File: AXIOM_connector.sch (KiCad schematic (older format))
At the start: 12 parts, among them U1001 BR24G04NUX

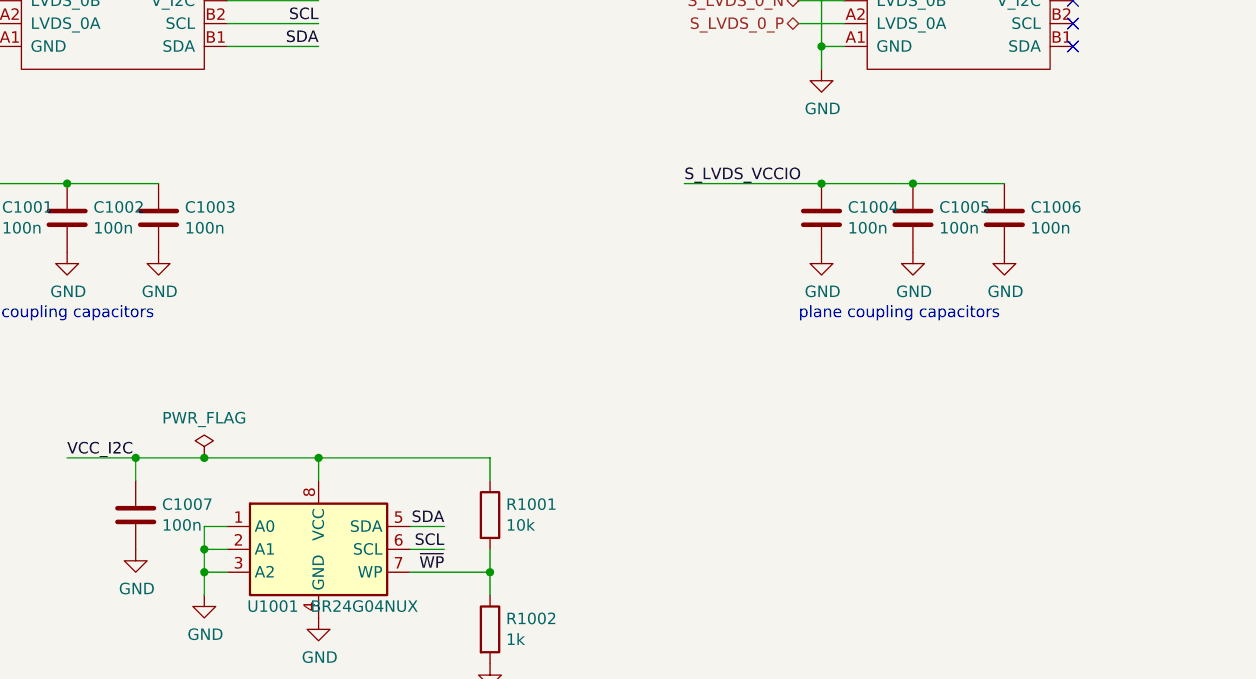
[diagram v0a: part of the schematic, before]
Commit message: route +3V3 net and add bypass capacitor
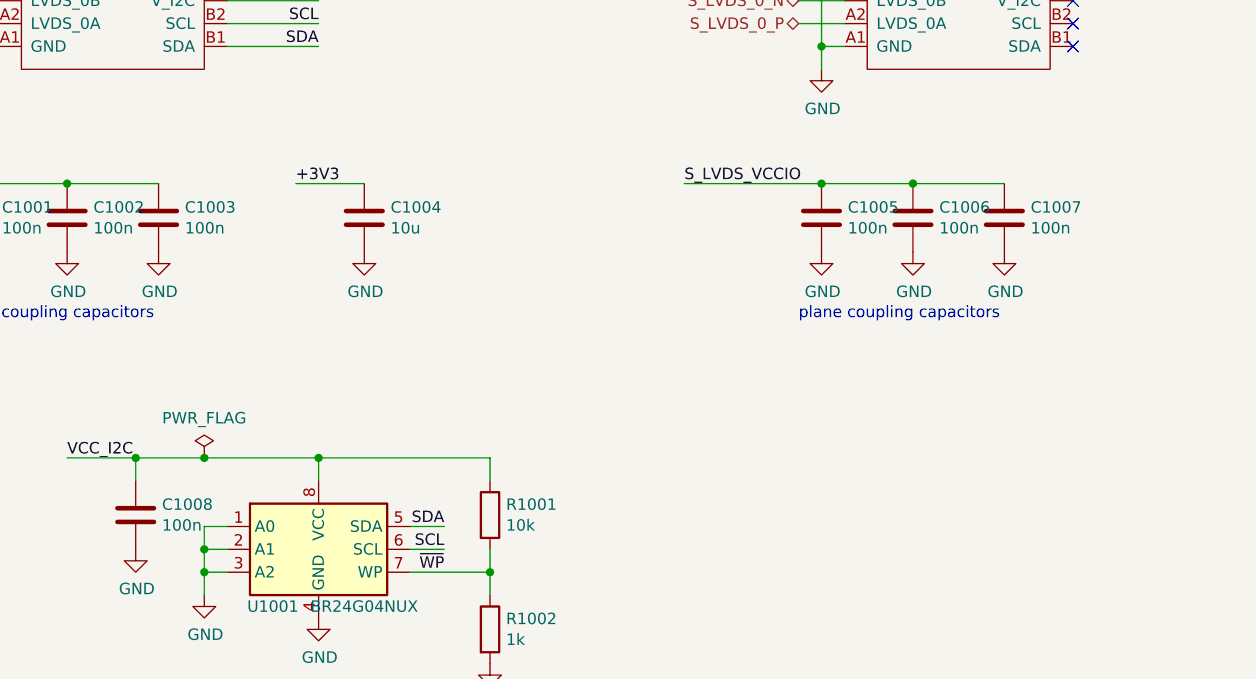
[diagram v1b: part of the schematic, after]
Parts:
- added C1004: 10u, Capacitor_SMD:C_0402_1005Metric, symbol Device:C
- renumbered C1004 to C1005, C1005 to C1006, C1006 to C1007, C1007 to C1008
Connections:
- net +3V3: now also C1004.1
- net GND: now also C1004.2
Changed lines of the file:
@@
 $EndComp
 $Comp
-L power:GND #PWR01013
+L power:GND #PWR01014
 U 1 1 5AFBF1A7
 P 4400 6800
-F 0 "#PWR01013" H 4400 6550 50  0001 C CNN
+F 0 "#PWR01014" H 4400 6550 50  0001 C CNN
 F 1 "GND" H 4405 6627 50  0000 C CNN
 F 2 "" H 4400 6800 50  0001 C CNN
@@
 $EndComp
 $Comp
-L power:GND #PWR01012
+L power:GND #PWR01013
 U 1 1 5AFBF1E7
 P 3900 6700
-F 0 "#PWR01012" H 3900 6450 50  0001 C CNN
+F 0 "#PWR01013" H 3900 6450 50  0001 C CNN
 F 1 "GND" H 3905 6527 50  0000 C CNN
 F 2 "" H 3900 6700 50  0001 C CNN
@@
 	3900 6600 3900 6700
 $Comp
-L Device:C C1007
+L Device:C C1008
 U 1 1 5AFC04F5
 P 3600 6350
-F 0 "C1007" H 3715 6396 50  0000 L CNN
+F 0 "C1008" H 3715 6396 50  0000 L CNN
 F 1 "100n" H 3715 6305 50  0000 L CNN
 F 2 "Capacitor_SMD:C_0402_1005Metric" H 3638 6200 50  0001 C CNN
@@
 $EndComp
 $Comp
-L power:GND #PWR01011
+L power:GND #PWR01012
 U 1 1 5AFC0567
 P 3600 6500
-F 0 "#PWR01011" H 3600 6250 50  0001 C CNN
+F 0 "#PWR01012" H 3600 6250 50  0001 C CNN
 F 1 "GND" H 3605 6327 50  0000 C CNN
 F 2 "" H 3600 6500 50  0001 C CNN
@@
 $EndComp
 $Comp
-L power:GND #PWR01014
+L power:GND #PWR01015
 U 1 1 5AFC3D07
 P 5150 7000
-F 0 "#PWR01014" H 5150 6750 50  0001 C CNN
+F 0 "#PWR01015" H 5150 6750 50  0001 C CNN
 F 1 "GND" H 5155 6827 50  0000 C CNN
 F 2 "" H 5150 7000 50  0001 C CNN
@@
 Connection ~ 3300 4900
 $Comp
-L Device:C C1004
+L Device:C C1005
 U 1 1 5B9999D8
 P 6600 5050
-F 0 "C1004" H 6715 5096 50  0000 L CNN
+F 0 "C1005" H 6715 5096 50  0000 L CNN
 F 1 "100n" H 6715 5005 50  0000 L CNN
 F 2 "Capacitor_SMD:C_0402_1005Metric" H 6638 4900 50  0001 C CNN
@@
 $EndComp
 $Comp
-L power:GND #PWR01008
+L power:GND #PWR01009
 U 1 1 5B9999DE
 P 6600 5200
-F 0 "#PWR01008" H 6600 4950 50  0001 C CNN
+F 0 "#PWR01009" H 6600 4950 50  0001 C CNN
 F 1 "GND" H 6605 5027 50  0000 C CNN
 F 2 "" H 6600 5200 50  0001 C CNN
@@
 	6000 4900 6600 4900
 $Comp
-L Device:C C1005
+L Device:C C1006
 U 1 1 5B9999E6
 P 7000 5050
-F 0 "C1005" H 7115 5096 50  0000 L CNN
+F 0 "C1006" H 7115 5096 50  0000 L CNN
 F 1 "100n" H 7115 5005 50  0000 L CNN
 F 2 "Capacitor_SMD:C_0402_1005Metric" H 7038 4900 50  0001 C CNN
@@
 $EndComp
 $Comp
-L power:GND #PWR01009
+L power:GND #PWR01010
 U 1 1 5B9999EC
 P 7000 5200
-F 0 "#PWR01009" H 7000 4950 50  0001 C CNN
+F 0 "#PWR01010" H 7000 4950 50  0001 C CNN
 F 1 "GND" H 7005 5027 50  0000 C CNN
 F 2 "" H 7000 5200 50  0001 C CNN
@@
 $EndComp
 $Comp
-L Device:C C1006
+L Device:C C1007
 U 1 1 5B9999F2
 P 7400 5050
-F 0 "C1006" H 7515 5096 50  0000 L CNN
+F 0 "C1007" H 7515 5096 50  0000 L CNN
 F 1 "100n" H 7515 5005 50  0000 L CNN
 F 2 "Capacitor_SMD:C_0402_1005Metric" H 7438 4900 50  0001 C CNN
@@
 $EndComp
 $Comp
-L power:GND #PWR01010
+L power:GND #PWR01011
 U 1 1 5B9999F8
 P 7400 5200
-F 0 "#PWR01010" H 7400 4950 50  0001 C CNN
+F 0 "#PWR01011" H 7400 4950 50  0001 C CNN
 F 1 "GND" H 7405 5027 50  0000 C CNN
 F 2 "" H 7400 5200 50  0001 C CNN
@@
 Text Notes 6500 5500 0    50   ~ 0
 plane coupling capacitors
+Wire Wire Line
+	4600 4900 4300 4900
+Text Label 4300 4900 0    50   ~ 0
++3V3
+$Comp
+L Device:C C1004
+U 1 1 5B4BBC86
+P 4600 5050
+F 0 "C1004" H 4715 5096 50  0000 L CNN
+F 1 "10u" H 4715 5005 50  0000 L CNN
+F 2 "Capacitor_SMD:C_0402_1005Metric" H 4638 4900 50  0001 C CNN
+F 3 "~" H 4600 5050 50  0001 C CNN
+	1    4600 5050
+	1    0    0    -1
+$EndComp
+$Comp
+L power:GND #PWR01008
+U 1 1 5B4BBCC0
+P 4600 5200
+F 0 "#PWR01008" H 4600 4950 50  0001 C CNN
+F 1 "GND" H 4605 5027 50  0000 C CNN
+F 2 "" H 4600 5200 50  0001 C CNN
+F 3 "" H 4600 5200 50  0001 C CNN
+	1    4600 5200
+	1    0    0    -1
+$EndComp
 $EndSCHEMATC

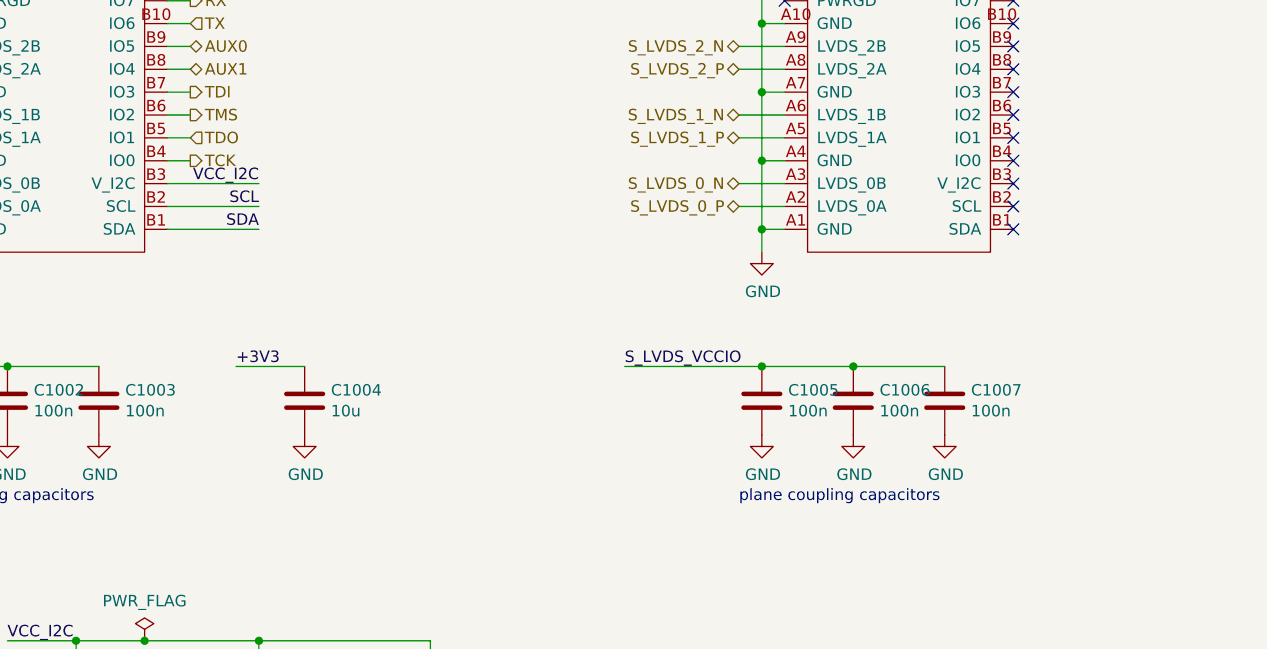
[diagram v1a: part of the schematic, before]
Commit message: move eeprom to south conector
also move the 5v->1,8v stepdown a bit to have space for the eeprom
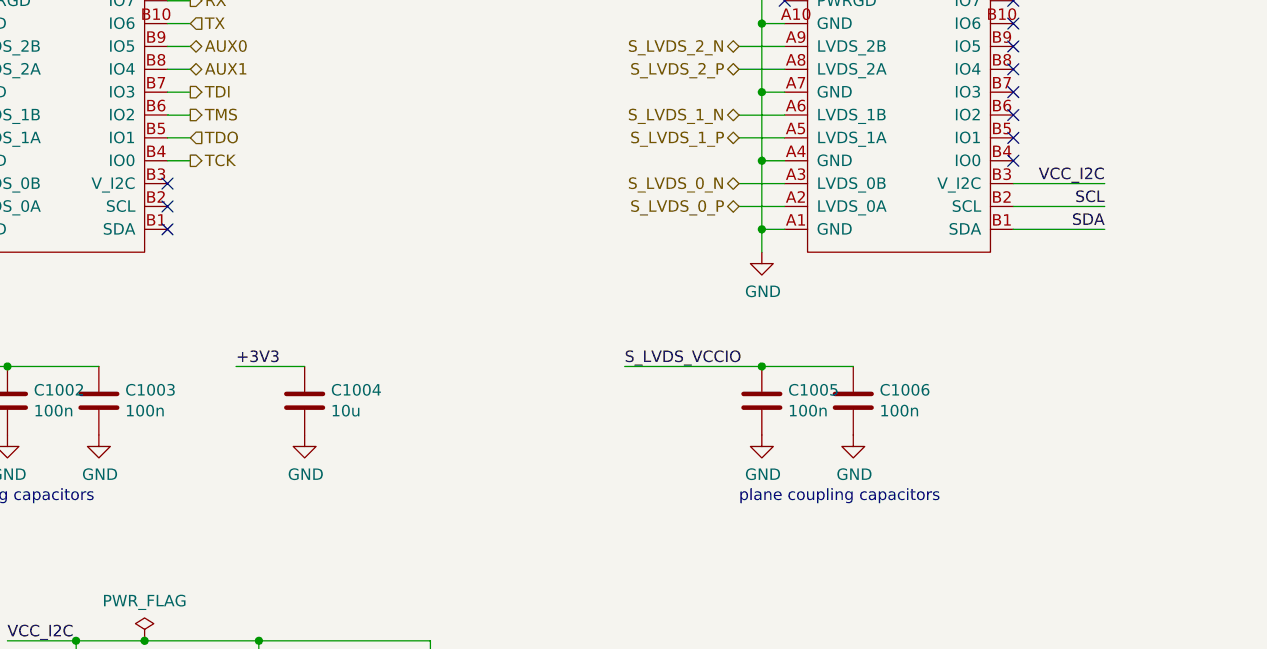
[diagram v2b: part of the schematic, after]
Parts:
- removed C1007: 100n, Capacitor_SMD:C_0402_1005Metric, symbol Device:C
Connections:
- net SCL: now also AXIOM_SOUTH1001.B2 (SCL); no longer AXIOM_NORTH1001.B2 (SCL)
- net SDA: now also AXIOM_SOUTH1001.B1 (SDA); no longer AXIOM_NORTH1001.B1 (SDA)
- net VCC_I2C: now also AXIOM_SOUTH1001.B3 (V_I2C); no longer AXIOM_NORTH1001.B3 (V_I2C)
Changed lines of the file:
@@
 EESchema Schematic File Version 4
 LIBS:AXIOM-photonSDI-hw-cache
-EELAYER 26 0
+EELAYER 29 0
 EELAYER END
 $Descr A4 11693 8268
@@
 Wire Wire Line
 	7700 2800 7800 2800
-NoConn ~ 7700 4300
-NoConn ~ 7700 4200
-NoConn ~ 7700 4100
-Wire Wire Line
-	4400 4300 4000 4300
-Wire Wire Line
-	4400 4200 4000 4200
-Wire Wire Line
-	4400 4100 4000 4100
-Text Label 4400 4100 2    50   ~ 0
+Wire Wire Line
+	8100 4300 7700 4300
+Wire Wire Line
+	8100 4200 7700 4200
+Wire Wire Line
+	8100 4100 7700 4100
+Text Label 8100 4100 2    50   ~ 0
 VCC_I2C
-Text Label 4400 4200 2    50   ~ 0
+Text Label 8100 4200 2    50   ~ 0
 SCL
-Text Label 4400 4300 2    50   ~ 0
+Text Label 8100 4300 2    50   ~ 0
 SDA
 $Comp
@@
 	1    0    0    -1
 $EndComp
-$Comp
-L Device:C C1007
-U 1 1 5B9999F2
-P 7400 5050
-F 0 "C1007" H 7515 5096 50  0000 L CNN
-F 1 "100n" H 7515 5005 50  0000 L CNN
-F 2 "Capacitor_SMD:C_0402_1005Metric" H 7438 4900 50  0001 C CNN
-F 3 "~" H 7400 5050 50  0001 C CNN
-	1    7400 5050
-	1    0    0    -1
-$EndComp
-$Comp
-L power:GND #PWR01011
-U 1 1 5B9999F8
-P 7400 5200
-F 0 "#PWR01011" H 7400 4950 50  0001 C CNN
-F 1 "GND" H 7405 5027 50  0000 C CNN
-F 2 "" H 7400 5200 50  0001 C CNN
-F 3 "" H 7400 5200 50  0001 C CNN
-	1    7400 5200
-	1    0    0    -1
-$EndComp
 Wire Wire Line
 	6600 4900 7000 4900
 Connection ~ 6600 4900
-Wire Wire Line
-	7000 4900 7400 4900
-Connection ~ 7000 4900
 Text Label 6000 4900 0    50   ~ 0
 S_LVDS_VCCIO
@@
 	1    0    0    -1
 $EndComp
+NoConn ~ 4000 4100
+NoConn ~ 4000 4200
+NoConn ~ 4000 4300
 $EndSCHEMATC

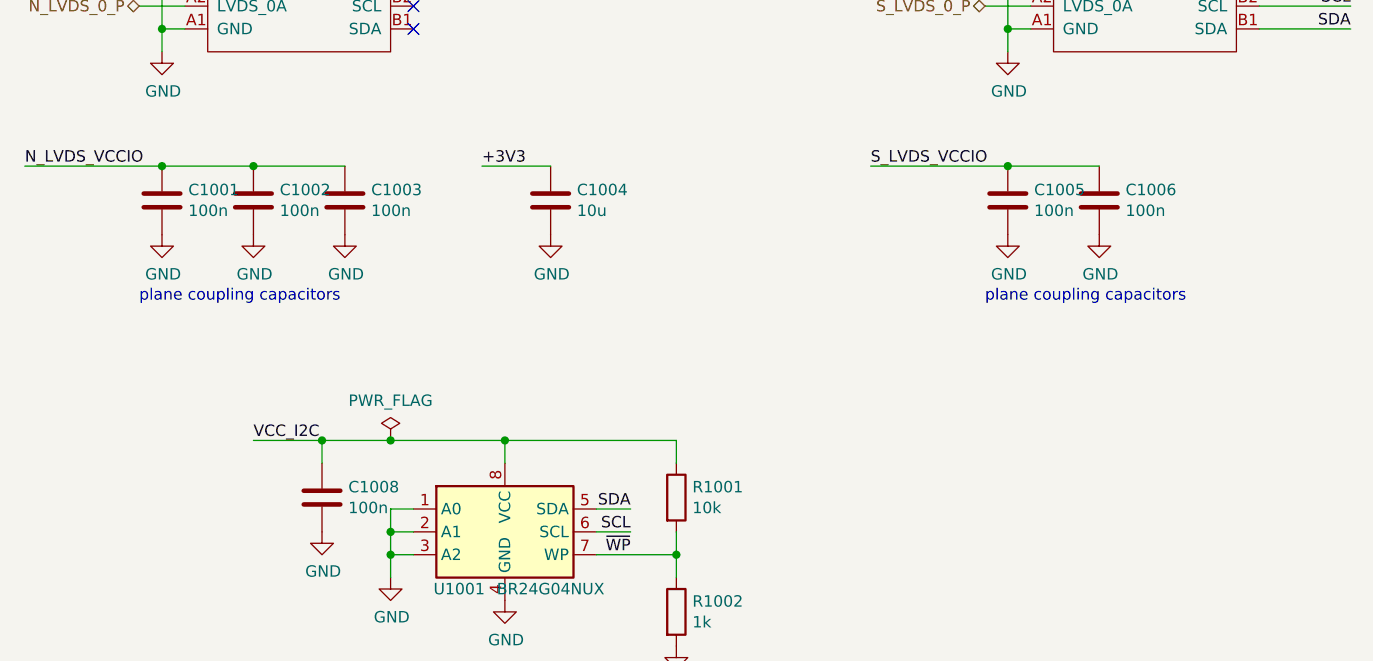
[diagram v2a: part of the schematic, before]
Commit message: rework plane coupling capacitors on axiom connector
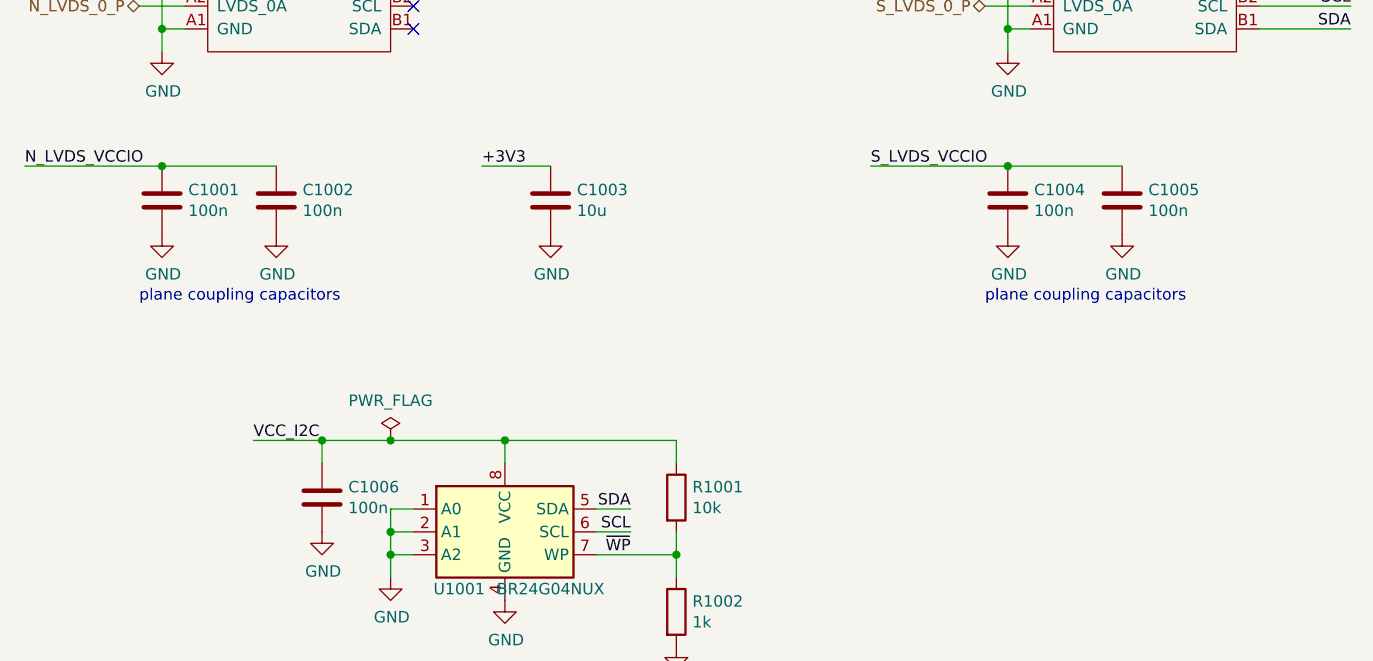
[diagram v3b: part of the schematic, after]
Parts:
- removed C1002: 100n, Capacitor_SMD:C_0402_1005Metric, symbol Device:C
- renumbered C1003 to C1002, C1004 to C1003, C1005 to C1004, C1006 to C1005, C1008 to C1006
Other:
- moved on the sheet: C1002, C1005
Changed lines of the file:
@@
 $EndComp
 $Comp
-L power:GND #PWR01014
+L power:GND #PWR01012
 U 1 1 5AFBF1A7
 P 4400 6800
-F 0 "#PWR01014" H 4400 6550 50  0001 C CNN
+F 0 "#PWR01012" H 4400 6550 50  0001 C CNN
 F 1 "GND" H 4405 6627 50  0000 C CNN
 F 2 "" H 4400 6800 50  0001 C CNN
@@
 $EndComp
 $Comp
-L power:GND #PWR01013
+L power:GND #PWR01011
 U 1 1 5AFBF1E7
 P 3900 6700
-F 0 "#PWR01013" H 3900 6450 50  0001 C CNN
+F 0 "#PWR01011" H 3900 6450 50  0001 C CNN
 F 1 "GND" H 3905 6527 50  0000 C CNN
 F 2 "" H 3900 6700 50  0001 C CNN
@@
 	3900 6600 3900 6700
 $Comp
-L Device:C C1008
+L Device:C C1006
 U 1 1 5AFC04F5
 P 3600 6350
-F 0 "C1008" H 3715 6396 50  0000 L CNN
+F 0 "C1006" H 3715 6396 50  0000 L CNN
 F 1 "100n" H 3715 6305 50  0000 L CNN
 F 2 "Capacitor_SMD:C_0402_1005Metric" H 3638 6200 50  0001 C CNN
@@
 $EndComp
 $Comp
-L power:GND #PWR01012
+L power:GND #PWR01010
 U 1 1 5AFC0567
 P 3600 6500
-F 0 "#PWR01012" H 3600 6250 50  0001 C CNN
+F 0 "#PWR01010" H 3600 6250 50  0001 C CNN
 F 1 "GND" H 3605 6327 50  0000 C CNN
 F 2 "" H 3600 6500 50  0001 C CNN
@@
 $EndComp
 $Comp
-L power:GND #PWR01015
+L power:GND #PWR01013
 U 1 1 5AFC3D07
 P 5150 7000
-F 0 "#PWR01015" H 5150 6750 50  0001 C CNN
+F 0 "#PWR01013" H 5150 6750 50  0001 C CNN
 F 1 "GND" H 5155 6827 50  0000 C CNN
 F 2 "" H 5150 7000 50  0001 C CNN
@@
 $Comp
 L Device:C C1002
-U 1 1 5B9079A6
-P 3300 5050
-F 0 "C1002" H 3415 5096 50  0000 L CNN
-F 1 "100n" H 3415 5005 50  0000 L CNN
-F 2 "Capacitor_SMD:C_0402_1005Metric" H 3338 4900 50  0001 C CNN
-F 3 "~" H 3300 5050 50  0001 C CNN
-	1    3300 5050
+U 1 1 5B90F3FB
+P 3400 5050
+F 0 "C1002" H 3515 5096 50  0000 L CNN
+F 1 "100n" H 3515 5005 50  0000 L CNN
+F 2 "Capacitor_SMD:C_0402_1005Metric" H 3438 4900 50  0001 C CNN
+F 3 "~" H 3400 5050 50  0001 C CNN
+	1    3400 5050
 	1    0    0    -1
 $EndComp
 $Comp
 L power:GND #PWR01006
-U 1 1 5B9079AD
-P 3300 5200
-F 0 "#PWR01006" H 3300 4950 50  0001 C CNN
-F 1 "GND" H 3305 5027 50  0000 C CNN
-F 2 "" H 3300 5200 50  0001 C CNN
-F 3 "" H 3300 5200 50  0001 C CNN
-	1    3300 5200
-	1    0    0    -1
-$EndComp
-$Comp
-L Device:C C1003
-U 1 1 5B90F3FB
-P 3700 5050
-F 0 "C1003" H 3815 5096 50  0000 L CNN
-F 1 "100n" H 3815 5005 50  0000 L CNN
-F 2 "Capacitor_SMD:C_0402_1005Metric" H 3738 4900 50  0001 C CNN
-F 3 "~" H 3700 5050 50  0001 C CNN
-	1    3700 5050
-	1    0    0    -1
-$EndComp
-$Comp
-L power:GND #PWR01007
 U 1 1 5B90F402
-P 3700 5200
-F 0 "#PWR01007" H 3700 4950 50  0001 C CNN
-F 1 "GND" H 3705 5027 50  0000 C CNN
-F 2 "" H 3700 5200 50  0001 C CNN
-F 3 "" H 3700 5200 50  0001 C CNN
-	1    3700 5200
-	1    0    0    -1
-$EndComp
-Wire Wire Line
-	2900 4900 3300 4900
+P 3400 5200
+F 0 "#PWR01006" H 3400 4950 50  0001 C CNN
+F 1 "GND" H 3405 5027 50  0000 C CNN
+F 2 "" H 3400 5200 50  0001 C CNN
+F 3 "" H 3400 5200 50  0001 C CNN
+	1    3400 5200
+	1    0    0    -1
+$EndComp
 Connection ~ 2900 4900
-Wire Wire Line
-	3300 4900 3700 4900
-Connection ~ 3300 4900
-$Comp
-L Device:C C1005
+$Comp
+L Device:C C1004
 U 1 1 5B9999D8
 P 6600 5050
-F 0 "C1005" H 6715 5096 50  0000 L CNN
+F 0 "C1004" H 6715 5096 50  0000 L CNN
 F 1 "100n" H 6715 5005 50  0000 L CNN
 F 2 "Capacitor_SMD:C_0402_1005Metric" H 6638 4900 50  0001 C CNN
@@
 $EndComp
 $Comp
-L power:GND #PWR01009
+L power:GND #PWR01008
 U 1 1 5B9999DE
 P 6600 5200
-F 0 "#PWR01009" H 6600 4950 50  0001 C CNN
+F 0 "#PWR01008" H 6600 4950 50  0001 C CNN
 F 1 "GND" H 6605 5027 50  0000 C CNN
 F 2 "" H 6600 5200 50  0001 C CNN
@@
 	6000 4900 6600 4900
 $Comp
-L Device:C C1006
+L Device:C C1005
 U 1 1 5B9999E6
-P 7000 5050
-F 0 "C1006" H 7115 5096 50  0000 L CNN
-F 1 "100n" H 7115 5005 50  0000 L CNN
-F 2 "Capacitor_SMD:C_0402_1005Metric" H 7038 4900 50  0001 C CNN
-F 3 "~" H 7000 5050 50  0001 C CNN
-	1    7000 5050
-	1    0    0    -1
-$EndComp
-$Comp
-L power:GND #PWR01010
+P 7100 5050
+F 0 "C1005" H 7215 5096 50  0000 L CNN
+F 1 "100n" H 7215 5005 50  0000 L CNN
+F 2 "Capacitor_SMD:C_0402_1005Metric" H 7138 4900 50  0001 C CNN
+F 3 "~" H 7100 5050 50  0001 C CNN
+	1    7100 5050
+	1    0    0    -1
+$EndComp
+$Comp
+L power:GND #PWR01009
 U 1 1 5B9999EC
-P 7000 5200
-F 0 "#PWR01010" H 7000 4950 50  0001 C CNN
-F 1 "GND" H 7005 5027 50  0000 C CNN
-F 2 "" H 7000 5200 50  0001 C CNN
-F 3 "" H 7000 5200 50  0001 C CNN
-	1    7000 5200
-	1    0    0    -1
-$EndComp
-Wire Wire Line
-	6600 4900 7000 4900
+P 7100 5200
+F 0 "#PWR01009" H 7100 4950 50  0001 C CNN
+F 1 "GND" H 7105 5027 50  0000 C CNN
+F 2 "" H 7100 5200 50  0001 C CNN
+F 3 "" H 7100 5200 50  0001 C CNN
+	1    7100 5200
+	1    0    0    -1
+$EndComp
+Wire Wire Line
+	6600 4900 7100 4900
 Connection ~ 6600 4900
 Text Label 6000 4900 0    50   ~ 0
@@
 +3V3
 $Comp
-L Device:C C1004
+L Device:C C1003
 U 1 1 5B4BBC86
 P 4600 5050
-F 0 "C1004" H 4715 5096 50  0000 L CNN
+F 0 "C1003" H 4715 5096 50  0000 L CNN
 F 1 "10u" H 4715 5005 50  0000 L CNN
 F 2 "Capacitor_SMD:C_0402_1005Metric" H 4638 4900 50  0001 C CNN
@@
 $EndComp
 $Comp
-L power:GND #PWR01008
+L power:GND #PWR01007
 U 1 1 5B4BBCC0
 P 4600 5200
-F 0 "#PWR01008" H 4600 4950 50  0001 C CNN
+F 0 "#PWR01007" H 4600 4950 50  0001 C CNN
 F 1 "GND" H 4605 5027 50  0000 C CNN
 F 2 "" H 4600 5200 50  0001 C CNN
@@
 NoConn ~ 4000 4200
 NoConn ~ 4000 4300
+Wire Wire Line
+	2900 4900 3400 4900
 $EndSCHEMATC
